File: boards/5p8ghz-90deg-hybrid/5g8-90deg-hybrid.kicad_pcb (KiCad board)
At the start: 4 copper layers, 25 x 39.5 mm, 7 parts, among them J1 SMA, J2 SMA, J3 SMA, J4 SMA, J5 SMA

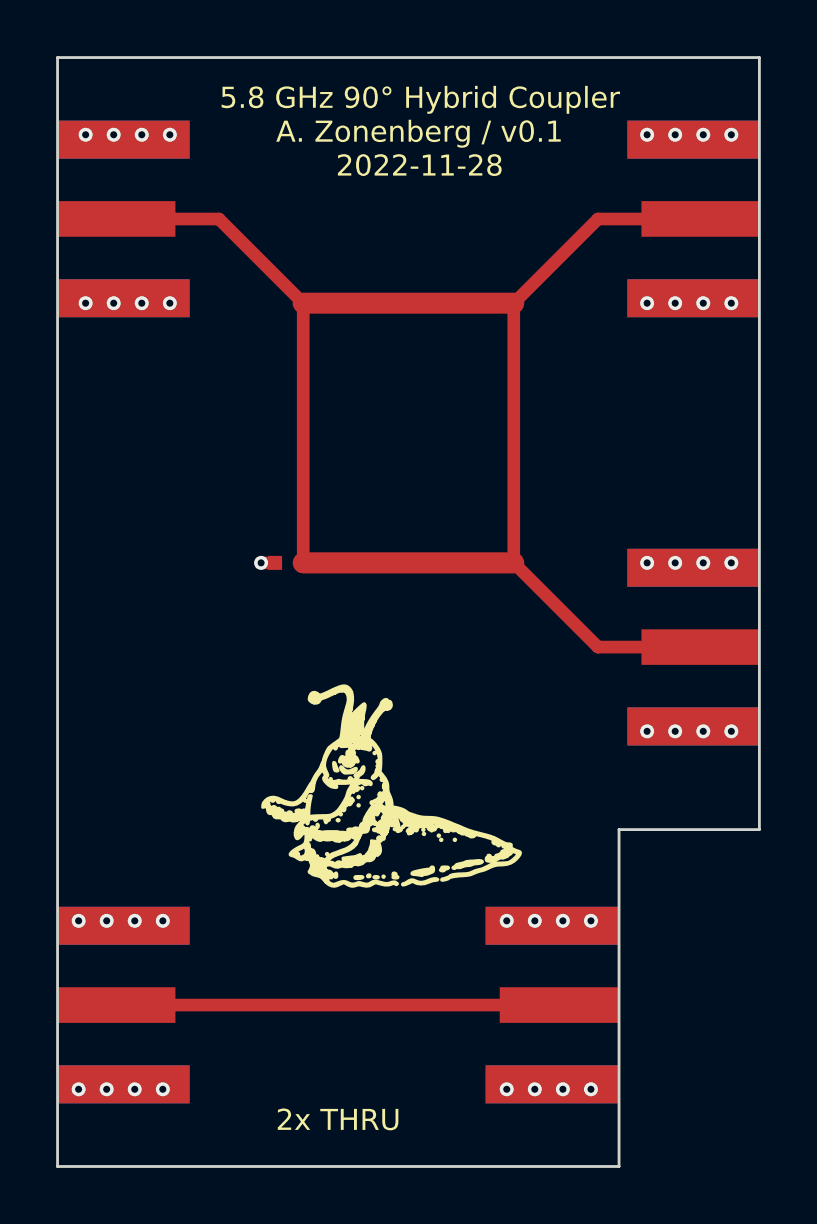
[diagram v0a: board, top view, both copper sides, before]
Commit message: Continued work on 90-deg hybrid model
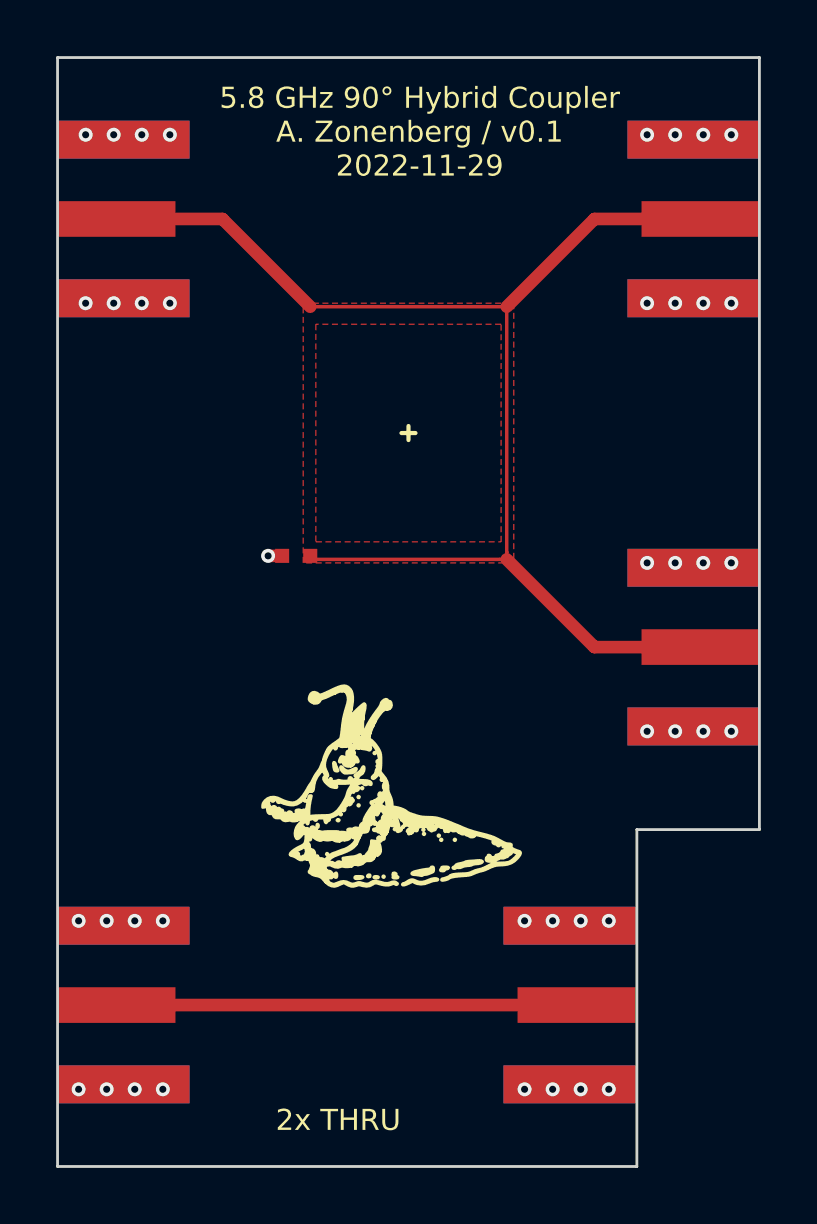
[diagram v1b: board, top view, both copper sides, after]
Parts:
- moved J2 0.63 mm to (120.6, 95.0)
- moved R1 0.35 mm to (108.5, 79.0)
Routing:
- net Net-(J1-Pad1): track 57.2 -> 47.6 mm
- added copper zone on F.Cu, net Net-(J1-Pad1)
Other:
- outline, holes or cut-outs redrawn
- board text added: "5.8 GHz 90° Hybrid Coupler A. Zonenberg / v0.1 2022-11-29"
- board text removed: "5.8 GHz 90° Hybrid Coupler A. Zonenberg / v0.1 2022-11-28"
